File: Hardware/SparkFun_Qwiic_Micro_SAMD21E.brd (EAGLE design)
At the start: 25.4 x 25.4 mm, 80 parts, among them Q1 3.1A/30V/105mΩ, U1 3.3V, U2 W25Q32FV, U3 ATSAMD21E18A-U

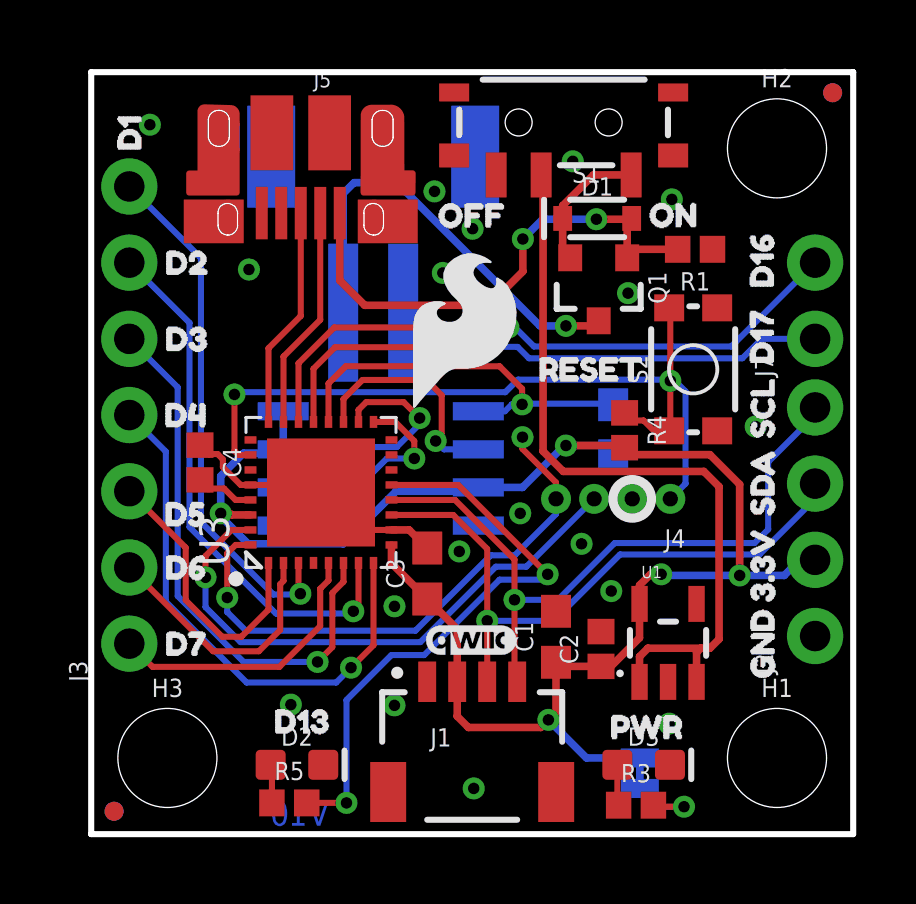
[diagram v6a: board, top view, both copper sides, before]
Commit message: Moves the EEPROM chip and Lipo connector away from each other every so slightly.
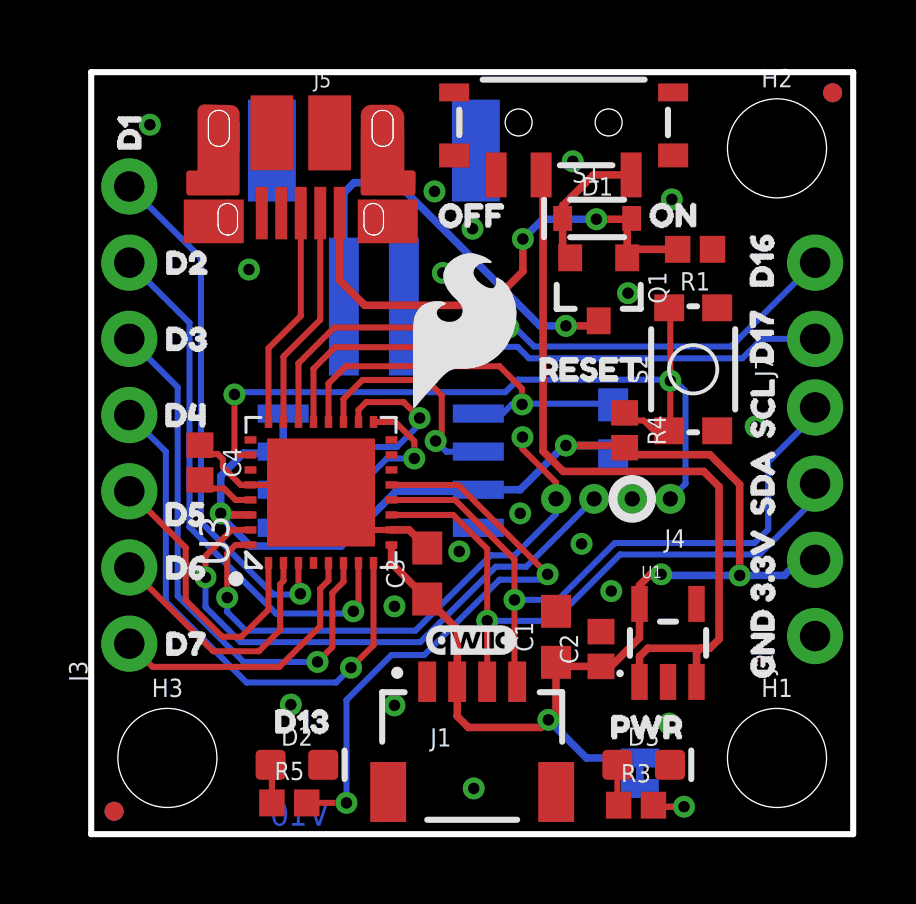
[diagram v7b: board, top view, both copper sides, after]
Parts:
- moved J6 0.20 mm to (9.42, 21.3)
- moved U2 0.08 mm to (9.65, 12.1)
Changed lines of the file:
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@@
 <layer number="19" name="Unrouted" color="6" fill="1" visible="yes" active="yes"/>
 <layer number="20" name="Dimension" color="15" fill="1" visible="yes" active="yes"/>
-<layer number="21" name="tPlace" color="16" fill="1" visible="yes" active="yes"/>
+<layer number="21" name="tPlace" color="16" fill="1" visible="no" active="yes"/>
 <layer number="22" name="bPlace" color="14" fill="1" visible="yes" active="yes"/>
 <layer number="23" name="tOrigins" color="15" fill="1" visible="yes" active="yes"/>
@@
 <layer number="49" name="Reference" color="13" fill="1" visible="yes" active="yes"/>
 <layer number="50" name="dxf" color="7" fill="1" visible="no" active="yes"/>
-<layer number="51" name="tDocu" color="6" fill="1" visible="yes" active="yes"/>
+<layer number="51" name="tDocu" color="6" fill="1" visible="no" active="yes"/>
 <layer number="52" name="bDocu" color="7" fill="1" visible="no" active="yes"/>
 <layer number="91" name="Nets" color="2" fill="1" visible="no" active="no"/>
@@
 <attribute name="VALUE" x="18.161" y="0.2032" size="0.6096" layer="27" font="vector" ratio="20" align="top-center"/>
 </element>
-<element name="U2" library="SparkFun-IC-Memory" package="SOIC-8" value="W25Q32FV" x="9.652" y="12.192" smashed="yes" rot="MR270">
-<attribute name="NAME" x="9.652" y="15.1765" size="0.6096" layer="26" font="vector" ratio="20" rot="MR0" align="bottom-center"/>
-<attribute name="PROD_ID" value="IC-13229" x="9.652" y="12.192" size="1.778" layer="28" font="vector" ratio="15" rot="MR270" display="off"/>
-<attribute name="VALUE" x="9.652" y="9.2075" size="0.6096" layer="28" font="vector" ratio="20" rot="MR180" align="bottom-center"/>
+<element name="U2" library="SparkFun-IC-Memory" package="SOIC-8" value="W25Q32FV" x="9.652" y="12.1158" smashed="yes" rot="MR270">
+<attribute name="NAME" x="9.652" y="15.1003" size="0.6096" layer="26" font="vector" ratio="20" rot="MR0" align="bottom-center"/>
+<attribute name="PROD_ID" value="IC-13229" x="9.652" y="12.1158" size="1.778" layer="28" font="vector" ratio="15" rot="MR270" display="off"/>
+<attribute name="VALUE" x="9.652" y="9.1313" size="0.6096" layer="28" font="vector" ratio="20" rot="MR180" align="bottom-center"/>
 </element>
 <element name="S1" library="SparkFun-Switches" package="SWITCH_SPST_SMD_A" value="" x="15.748" y="23.7236" smashed="yes">
@@
 <element name="U$19" library="buzzard_labels" package="OFF13" value="" x="16.8021" y="21.6408" smashed="yes" rot="MR0"/>
 <element name="TP2" library="SparkFun-Connectors" package="TP_15TH" value="TEST-POINTTP_15TH_THRU" x="15.8242" y="16.9418" smashed="yes"/>
-<element name="J6" library="SparkFun-Connectors" package="JST-2-SMD" value="" x="9.398" y="21.082" smashed="yes" rot="MR0">
-<attribute name="NAME" x="10.795" y="22.86" size="0.6096" layer="26" font="vector" ratio="20" rot="MR0"/>
-<attribute name="PROD_ID" value="CONN-11443" x="9.398" y="21.082" size="1.778" layer="28" font="vector" ratio="15" rot="MR0" display="off"/>
-<attribute name="SF_ID" value="PRT-08612" x="9.398" y="21.082" size="1.778" layer="28" font="vector" ratio="15" rot="MR0" display="off"/>
-<attribute name="VALUE" x="11.049" y="21.717" size="0.6096" layer="28" font="vector" ratio="20" rot="MR0"/>
+<element name="J6" library="SparkFun-Connectors" package="JST-2-SMD" value="" x="9.4234" y="21.2852" smashed="yes" rot="MR0">
+<attribute name="NAME" x="10.8204" y="23.0632" size="0.6096" layer="26" font="vector" ratio="20" rot="MR0"/>
+<attribute name="PROD_ID" value="CONN-11443" x="9.4234" y="21.2852" size="1.778" layer="28" font="vector" ratio="15" rot="MR0" display="off"/>
+<attribute name="SF_ID" value="PRT-08612" x="9.4234" y="21.2852" size="1.778" layer="28" font="vector" ratio="15" rot="MR0" display="off"/>
+<attribute name="VALUE" x="11.0744" y="21.9202" size="0.6096" layer="28" font="vector" ratio="20" rot="MR0"/>
 </element>
 <element name="U$1" library="D0" package="D00" value="" x="23.7236" y="11.6332" smashed="yes" rot="MR0"/>
@@
 <via x="4.318" y="10.6934" extent="1-16" drill="0.381"/>
 <wire x1="21.6154" y1="8.6233" x2="23.1013" y2="8.6233" width="0.254" layer="16"/>
-<wire x1="6.4008" y1="12.827" x2="6.4008" y2="14.097" width="0.254" layer="16"/>
+<wire x1="6.4008" y1="12.7508" x2="6.4008" y2="14.0208" width="0.254" layer="16"/>
 <wire x1="6.0198" y1="12.7" x2="5.08" y2="12.7" width="0.254" layer="16"/>
 <via x="15.24" y="3.81" extent="1-16" drill="0.381"/>
@@
 <wire x1="18.6436" y1="8.6614" x2="18.2778" y2="8.2956" width="0.254" layer="1"/>
 <wire x1="18.9992" y1="8.6614" x2="18.6436" y2="8.6614" width="0.254" layer="1"/>
-<wire x1="5.2324" y1="9.6774" x2="4.318" y2="10.5918" width="0.254" layer="16"/>
+<wire x1="5.3086" y1="9.6012" x2="4.318" y2="10.5918" width="0.254" layer="16"/>
 <wire x1="4.318" y1="10.5918" x2="4.318" y2="10.6934" width="0.254" layer="16"/>
-<wire x1="6.4008" y1="12.827" x2="6.2738" y2="12.7" width="0.2032" layer="16"/>
-<wire x1="6.2738" y1="12.7" x2="6.0198" y2="12.7" width="0.2032" layer="16"/>
-<wire x1="12.9032" y1="11.557" x2="14.3764" y2="11.557" width="0.254" layer="16"/>
+<wire x1="6.4008" y1="12.7508" x2="6.35" y2="12.7" width="0.2032" layer="16"/>
+<wire x1="6.35" y1="12.7" x2="6.0198" y2="12.7" width="0.2032" layer="16"/>
+<wire x1="12.9032" y1="11.4808" x2="14.3002" y2="11.4808" width="0.254" layer="16"/>
 <wire x1="15.7734" y1="12.954" x2="15.8242" y2="12.954" width="0.254" layer="16"/>
-<wire x1="14.3764" y1="11.557" x2="15.7734" y2="12.954" width="0.254" layer="16"/>
-<wire x1="12.9032" y1="11.557" x2="12.7762" y2="11.43" width="0.254" layer="16"/>
-<wire x1="12.7762" y1="11.43" x2="10.16" y2="11.43" width="0.254" layer="16"/>
-<wire x1="8.4074" y1="9.6774" x2="5.2324" y2="9.6774" width="0.254" layer="16"/>
-<wire x1="10.16" y1="11.43" x2="8.4074" y2="9.6774" width="0.254" layer="16"/>
+<wire x1="14.3002" y1="11.4808" x2="15.7734" y2="12.954" width="0.254" layer="16"/>
+<wire x1="12.9032" y1="11.4808" x2="12.8524" y2="11.43" width="0.254" layer="16"/>
+<wire x1="12.8524" y1="11.43" x2="10.16" y2="11.43" width="0.254" layer="16"/>
+<wire x1="8.3312" y1="9.6012" x2="5.3086" y2="9.6012" width="0.254" layer="16"/>
+<wire x1="10.16" y1="11.43" x2="8.3312" y2="9.6012" width="0.254" layer="16"/>
 <wire x1="14.986" y1="3.556" x2="15.24" y2="3.81" width="0.254" layer="1"/>
 <wire x1="12.573" y1="3.556" x2="14.986" y2="3.556" width="0.254" layer="1"/>
@@
 <wire x1="10.7696" y1="12.5222" x2="9.8552" y2="12.5222" width="0.2032" layer="16"/>
 <wire x1="10.7696" y1="12.5222" x2="10.7696" y2="13.1064" width="0.2032" layer="1"/>
-<wire x1="7.62" y1="10.287" x2="6.4008" y2="10.287" width="0.2032" layer="16"/>
-<wire x1="9.8552" y1="12.5222" x2="7.62" y2="10.287" width="0.2032" layer="16"/>
+<wire x1="7.5438" y1="10.2108" x2="6.4008" y2="10.2108" width="0.2032" layer="16"/>
+<wire x1="9.8552" y1="12.5222" x2="7.5438" y2="10.2108" width="0.2032" layer="16"/>
 <contactref element="U3" pad="PA16"/>
 <wire x1="10.136" y1="13.74" x2="9.41" y2="13.74" width="0.2032" layer="1"/>
@@
 <wire x1="10.9474" y1="13.6652" x2="10.9474" y2="13.8684" width="0.2032" layer="16"/>
 <wire x1="10.1854" y1="12.9032" x2="10.9474" y2="13.6652" width="0.2032" layer="16"/>
-<wire x1="9.1186" y1="12.9032" x2="7.7724" y2="11.557" width="0.2032" layer="16"/>
-<wire x1="7.7724" y1="11.557" x2="6.4008" y2="11.557" width="0.2032" layer="16"/>
+<wire x1="9.1186" y1="12.9032" x2="7.6962" y2="11.4808" width="0.2032" layer="16"/>
+<wire x1="7.6962" y1="11.4808" x2="6.4008" y2="11.4808" width="0.2032" layer="16"/>
 <contactref element="U3" pad="PA17"/>
 <wire x1="8.91" y1="14.1424" x2="8.91" y2="13.74" width="0.2032" layer="1"/>
@@
 <wire x1="11.684" y1="13.3096" x2="11.4808" y2="13.1064" width="0.2032" layer="1"/>
 <wire x1="11.684" y1="14.6304" x2="11.684" y2="13.3096" width="0.2032" layer="1"/>
-<wire x1="12.9032" y1="12.827" x2="11.7602" y2="12.827" width="0.2032" layer="16"/>
-<wire x1="11.7602" y1="12.827" x2="11.4808" y2="13.1064" width="0.2032" layer="16"/>
+<wire x1="12.9032" y1="12.7508" x2="11.8364" y2="12.7508" width="0.2032" layer="16"/>
+<wire x1="11.8364" y1="12.7508" x2="11.4808" y2="13.1064" width="0.2032" layer="16"/>
 <contactref element="U3" pad="PA18"/>
 <wire x1="8.41" y1="13.74" x2="8.41" y2="14.506" width="0.2032" layer="1"/>
@@
 <contactref element="R2" pad="1"/>
 <wire x1="14.3637" y1="14.3256" x2="14.0208" y2="14.3256" width="0.2032" layer="16"/>
-<wire x1="14.0208" y1="14.3256" x2="13.7922" y2="14.097" width="0.2032" layer="16"/>
-<wire x1="13.7922" y1="14.097" x2="12.9032" y2="14.097" width="0.2032" layer="16"/>
+<wire x1="14.0208" y1="14.3256" x2="13.716" y2="14.0208" width="0.2032" layer="16"/>
+<wire x1="13.716" y1="14.0208" x2="12.9032" y2="14.0208" width="0.2032" layer="16"/>
 <wire x1="17.36" y1="14.351" x2="17.399" y2="14.312" width="0.2032" layer="16"/>
 <wire x1="14.3383" y1="14.351" x2="17.36" y2="14.351" width="0.2032" layer="16"/>
@@
 <contactref element="Q1" pad="3"/>
 <wire x1="10.1854" y1="21.717" x2="8.763" y2="21.717" width="0.254" layer="16"/>
-<wire x1="8.763" y1="21.717" x2="8.398" y2="21.352" width="0.254" layer="16"/>
+<wire x1="8.763" y1="21.717" x2="8.4234" y2="21.3774" width="0.254" layer="16"/>
 <contactref element="TP2" pad="P$1"/>
 <wire x1="16.9164" y1="17.1118" x2="16.7464" y2="16.9418" width="0.254" layer="1"/>
@@
 <wire x1="14.9606" y1="16.9418" x2="10.1854" y2="21.717" width="0.254" layer="16"/>
 <contactref element="J6" pad="2"/>
-<wire x1="8.398" y1="21.352" x2="8.398" y2="17.382" width="0.254" layer="16"/>
+<wire x1="8.4234" y1="21.3774" x2="8.4234" y2="17.5852" width="0.254" layer="16"/>
 </signal>
 <signal name="V_USB">

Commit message: Moves 10k pull-up resistor on Flash CS line to top layer.
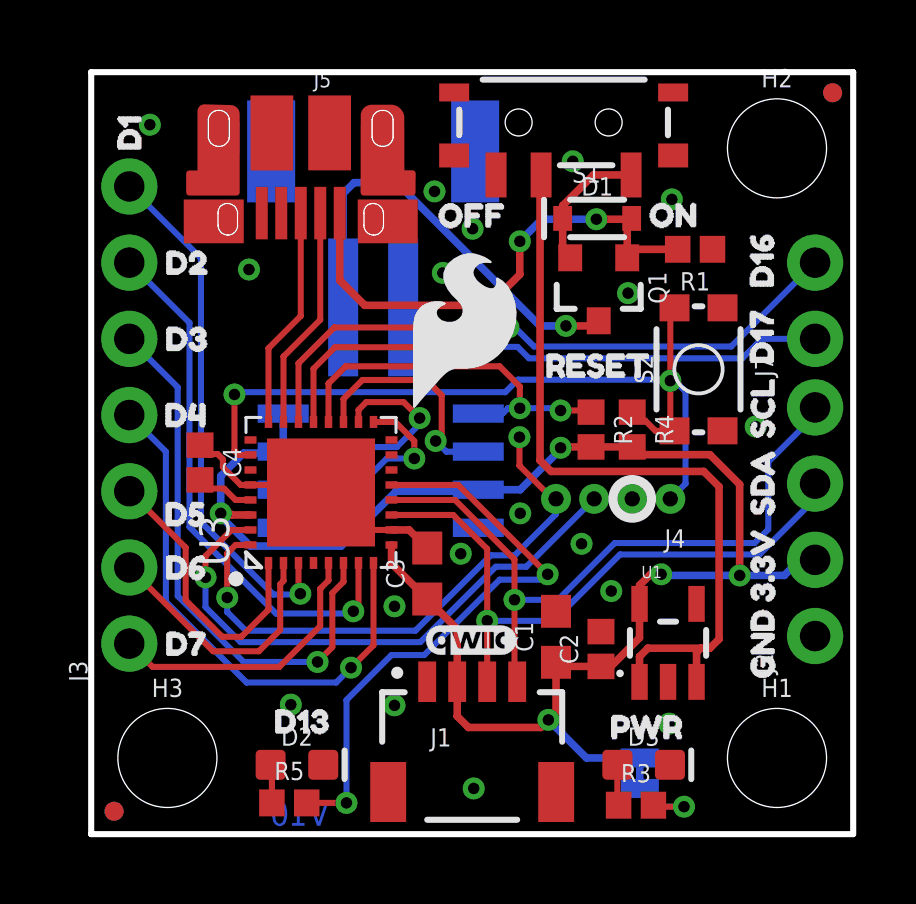
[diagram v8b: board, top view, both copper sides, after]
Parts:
- R2: device SparkFun-Resistors:0603 -> SparkFun-Resistors:0402
- moved R2 0.74 mm to (16.7, 13.5), flipped to the top
- moved U$21 0.26 mm to (14.5, 15.6)
- moved R4 0.26 mm to (18.0, 13.5)
- moved S2 0.18 mm to (20.2, 15.5)
- moved TP3 0.10 mm to (14.3, 13.2)
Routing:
- net 3.3V: track 57.2 -> 55.4 mm
- net FLASH_CS: track 13.5 -> 12.8 mm, vias 1 -> 2
